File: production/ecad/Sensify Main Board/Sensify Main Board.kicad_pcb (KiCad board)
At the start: 4 copper layers, 142 parts, among them J1 1-2834011-3, J2 1-2834011-2, J3 1332645, J4 0532611271, J6 Conn_01x02_Socket, J7 Conn_01x02_Socket, J8 Conn_01x02_Socket, J9 Conn_01x02_Socket, Q1 2N700, Q2 PMPB13XNE,115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

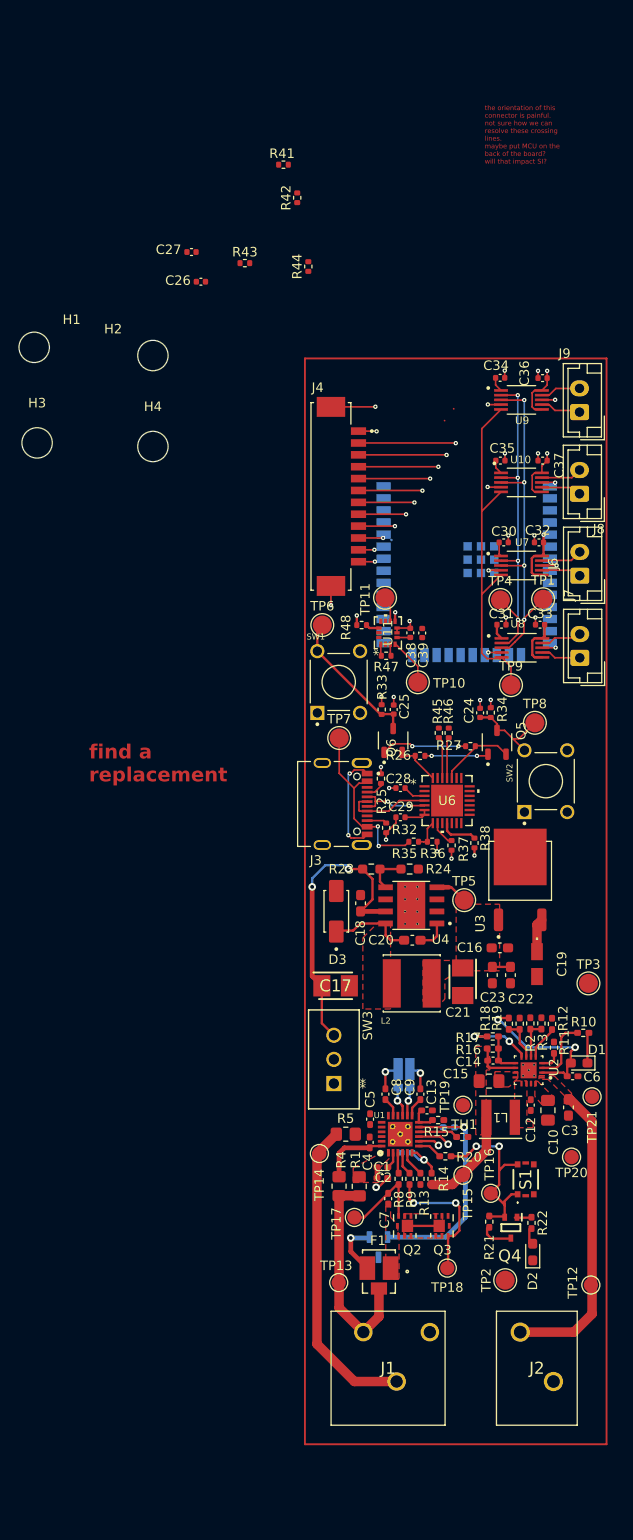
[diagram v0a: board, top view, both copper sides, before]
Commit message: main board layout
made some changes to routing, connected up parts of the MCU
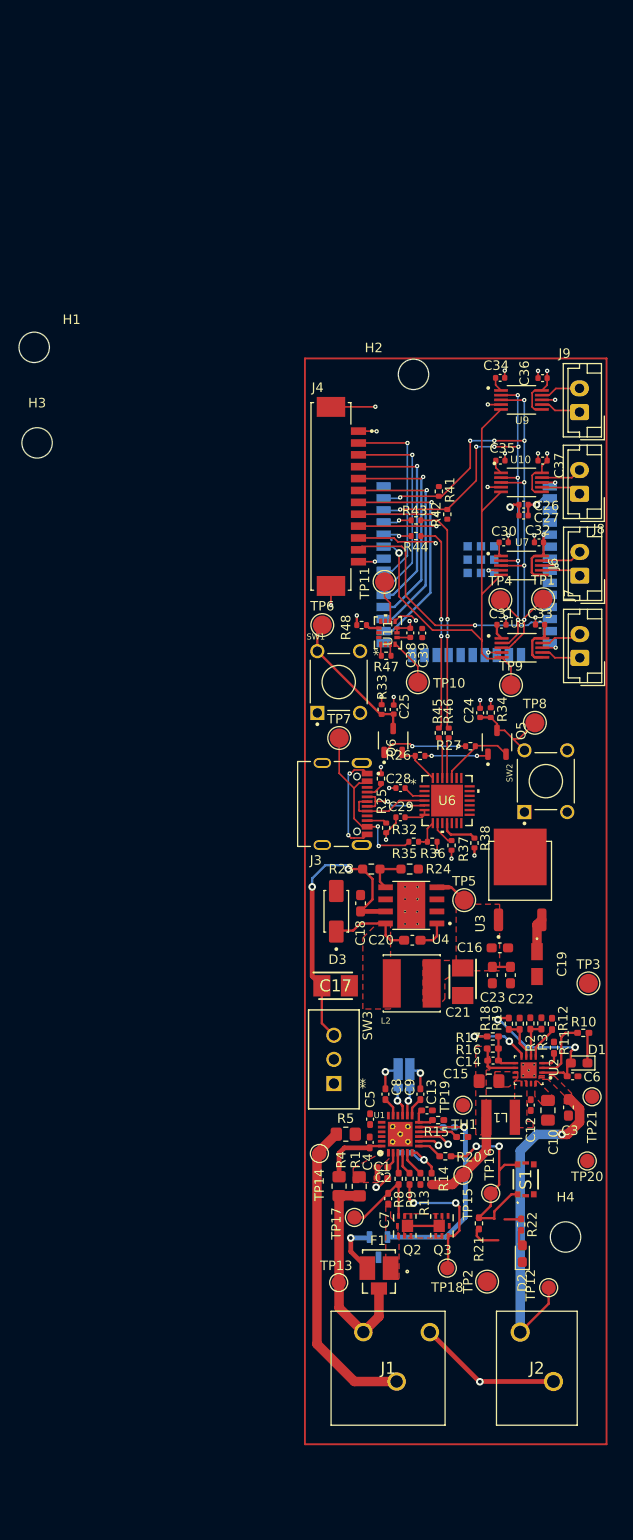
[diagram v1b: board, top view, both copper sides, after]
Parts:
- removed Q4: BSS223PWH6327XTSA1, Sensify Footprints:SOT65P210X100-3N
- moved H4 93.9 mm to (154.9, 162.1)
- moved C27 44.6 mm to (150.5, 86.1), turned to 180 degrees
- moved C26 41.3 mm to (150.5, 85.0), turned to 180 degrees
- moved R41 38.1 mm to (141.6, 83.6), turned to -90 degrees
- moved R42 36.9 mm to (142.5, 86.0)
- moved R43 32.5 mm to (139.2, 86.6), turned to 180 degrees
- moved R44 30.5 mm to (139.2, 88.3), turned to 180 degrees
- moved H2 27.5 mm to (138.9, 71.3)
- moved TP12 4.45 mm to (153.2, 167.4)
- moved TP2 1.91 mm to (146.7, 166.8)
- moved TP20 1.70 mm to (157.2, 154.1)
- moved TP11 1.68 mm to (135.9, 93.1)
- moved R22 1.10 mm to (150.3, 160.8)
- moved D2 1.10 mm to (150.4, 163.8)
- moved R21 1.10 mm to (145.8, 160.6)
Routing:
- net NovelDetect: track 1.68 -> 26.8 mm
- net UART_RXD: track 0.00 -> 24.1 mm, vias 0 -> 2
- net UART_TXD: track 0.00 -> 22.3 mm, vias 0 -> 2
- net SCL: track 37.7 -> 56.8 mm, vias 5 -> 9
- net SDA: track 41.9 -> 60.9 mm, vias 5 -> 9
- net NovelMechPin7: track 5.90 -> 23.9 mm
- net HAPTICS_EN: track 38.0 -> 55.6 mm, vias 0 -> 1
- net GND: track 54.5 -> 72.0 mm, vias 30 -> 32
- net NovelMechPin6: track 6.74 -> 23.2 mm
- net NovelMechPin5: track 7.54 -> 23.0 mm
- net NovelMechPin4: track 8.44 -> 21.8 mm
- net NovelMechPin3: track 9.28 -> 20.9 mm
- net NovelMechPin2: track 10.2 -> 20.2 mm
- net NovelMechPin10: track 2.59 -> 8.36 mm
- net +3V3: track 19.9 -> 25.2 mm, vias 7 -> 8
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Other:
- board text removed: "find a replacement"
- board text removed: "the orientation of this connector is painful. not sure how we can resolve these crossing lines. maybe put MCU on the back of the board? will that impact SI?"

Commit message: added last mounting hole and moved aronud R7 to make room for MH
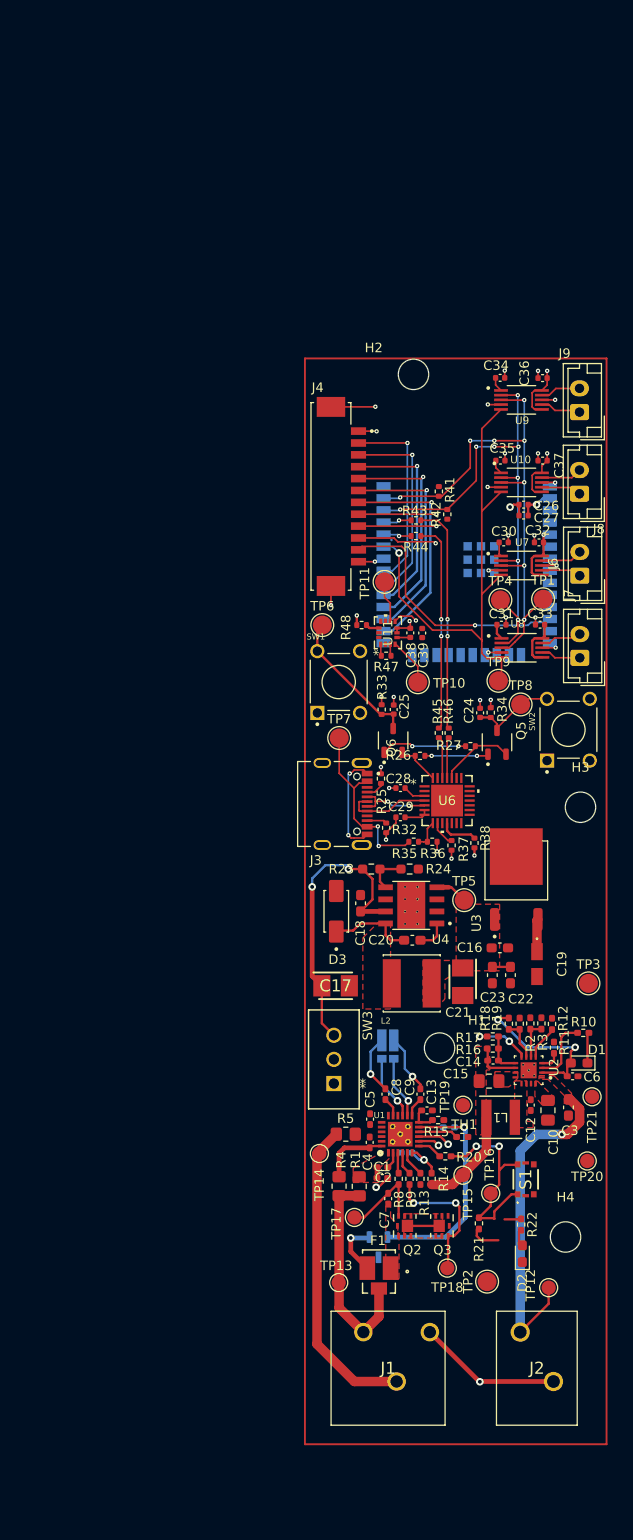
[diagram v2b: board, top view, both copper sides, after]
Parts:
- moved H1 85.2 mm to (141.7, 142.2)
- moved H3 68.9 mm to (156.5, 116.8)
- moved SW2 5.91 mm to (155.2, 108.7)
- moved R7 3.47 mm to (136.2, 142.0)
- moved TP8 2.44 mm to (150.2, 106.0)
- moved TP9 1.40 mm to (147.9, 103.5)
- moved U3 0.41 mm to (149.8, 124.5)
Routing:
- net GND: track 72.0 -> 78.4 mm
- net Net-(U1-CSP): track 3.03 -> 6.89 mm
- net Net-(U1-CSN): track 2.89 -> 6.66 mm
- net Net-(U2-FB_GND): track 7.42 -> 6.30 mm
- net HAPTICS_EN: track 55.6 -> 54.8 mm

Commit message: Main Board Layout
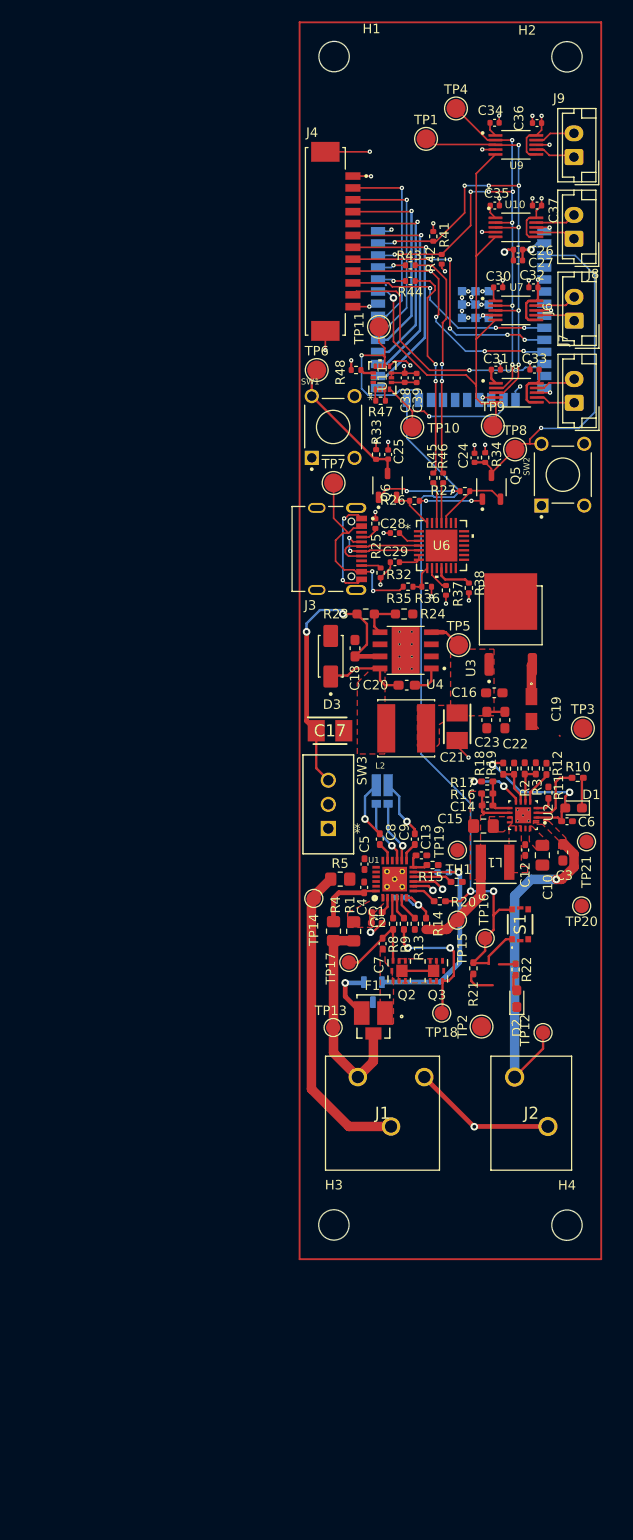
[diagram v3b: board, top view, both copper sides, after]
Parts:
- moved H1 105.0 mm to (130.6, 37.8)
- moved TP4 52.0 mm to (143.4, 43.3)
- moved H3 51.1 mm to (130.6, 160.8)
- moved TP1 50.0 mm to (140.3, 46.5)
- moved H2 37.1 mm to (155.1, 37.8)
- moved C16 26.9 mm to (147.4, 104.8)
- moved C15 26.9 mm to (146.3, 118.8)
- moved C18 26.9 mm to (132.8, 100.1)
- moved C19 26.9 mm to (151.4, 106.5)
- moved C20 26.9 mm to (138.2, 104.0)
- moved C21 26.9 mm to (143.5, 108.4)
- moved C22 26.9 mm to (148.6, 107.7)
- moved C23 26.9 mm to (146.7, 107.7)
- moved C25 26.9 mm to (136.3, 79.7)
- moved C28 26.9 mm to (137.0, 88.0)
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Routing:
- net BMS_ALERT: track 22.0 -> 81.7 mm
- net EN: track 9.53 -> 38.7 mm, vias 0 -> 1
- net GND: track 78.4 -> 100.2 mm, vias 32 -> 43
- net NovelMechPin8: track 8.20 -> 27.9 mm, vias 1 -> 5
- net NovelMechPin9: track 8.21 -> 26.7 mm, vias 1 -> 4
- net NovelMechPin10: track 8.36 -> 22.8 mm, vias 1 -> 3
- net INTERRUPT2_IMU: track 4.40 -> 17.9 mm, vias 0 -> 1
- net INTERRUPT1_IMU: track 5.21 -> 16.3 mm, vias 0 -> 1
- net SDA: track 60.9 -> 65.6 mm
- net SCL: track 56.8 -> 59.9 mm
- net +3V3: track 25.1 -> 28.1 mm, vias 8 -> 10
- net USB_D-: track 8.05 -> 10.2 mm
- net FLASHING_VBUS_5V: track 19.3 -> 21.4 mm
- net USB_D+: track 9.22 -> 10.3 mm
- net UART_TXD: track 22.3 -> 22.9 mm

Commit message: routing generally done
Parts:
- removed C13: 0.47u, Capacitor_SMD:C_0402_1005Metric_Pad0.74x0.62mm_HandSolder
- removed R12, R3: 0, Resistor_SMD:R_0402_1005Metric_Pad0.72x0.64mm_HandSolder
- added Q4: BSS223PWH6327XTSA1, Sensify Footprints:SOT65P210X100-3N, F.Cu at (148.0, 161.2)
- R7: moved to F.Cu
- moved H3 88.1 mm to (99.3, 78.5)
- moved TP4 52.0 mm to (148.1, 95.0)
- moved TP1 49.9 mm to (152.7, 94.8)
- moved H1 44.0 mm to (99.0, 68.4)
- moved H2 37.1 mm to (138.9, 71.3)
- moved SW2 32.3 mm to (152.9, 114.1)
- moved R7 30.9 mm to (137.5, 146.0), turned to 180 degrees
- moved TP8 28.9 mm to (151.7, 108.0)
- moved C29 27.5 mm to (138.9, 118.4), turned to -90 degrees
- moved C9 27.4 mm to (139.6, 147.6)
- moved TP9 27.4 mm to (149.2, 104.0)
- moved C8 27.3 mm to (135.4, 147.5)
- moved C28 27.3 mm to (138.8, 115.2), turned to -90 degrees
- moved R38 27.0 mm to (145.8, 120.7)
- moved R24 27.0 mm to (139.0, 123.5)
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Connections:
- R15 pad 1: AOLDO_OUT -> Net-(U1-AOLDO)
- R2 pad 1: AOLDO_OUT -> Net-(U2-~{EN})
- R2 pad 2: /BMS/CHARGER_EN -> GND
- R7 pad 2: Net-(U1-CSP) -> Net-(U1-CSN)
- R7 pad 3: Net-(U1-CSN) -> Net-(U1-CSP)
- U1 pad 12: AOLDO_OUT -> Net-(U1-AOLDO)
- U2 pad 5: Net-(U2-POL) -> unconnected-(U2-POL-Pad5)
- U2 pad 6: /BMS/CHARGER_EN -> Net-(U2-~{EN})
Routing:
- net GND: track 100.2 -> 180.9 mm, vias 43 -> 67
- net SDA: track 65.6 -> 141.5 mm, vias 9 -> 11
- net SCL: track 59.9 -> 134.6 mm, vias 9 -> 11
- net PACK+: track 16.3 -> 44.4 mm
- net INTERRUPT2_IMU: track 17.9 -> 4.40 mm, vias 1 -> 0
- net +3V3: track 28.1 -> 38.6 mm, vias 10 -> 14
- net Net-(U2-PMID): track 0.00 -> 9.96 mm
- net IO0: track 15.3 -> 23.6 mm
- net Net-(U1-TH1): track 4.20 -> 11.9 mm
- net USB_9V+: track 35.6 -> 41.9 mm
- net Net-(U1-CELL1): track 0.00 -> 6.14 mm
- net Net-(U1-CSN): track 6.66 -> 2.03 mm, vias 1 -> 0
- net Net-(U1-CSP): track 6.89 -> 2.34 mm, vias 1 -> 0
- net /BMS/CHARGER_EN: track 4.15 -> 0.00 mm
- net +5V: track 30.8 -> 34.8 mm, vias 4 -> 6
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- added copper zone on In1.Cu, net +3V3
- added copper zone on In1.Cu, net +5V
- added copper zone on B.Cu, net GND
- added copper zone on In2.Cu, net GND
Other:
- board outline added: 31.8 x 114.3 mm

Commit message: mounting holes...
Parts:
- moved H1 124.2 mm to (131.0, 188.4)
- moved H3 34.3 mm to (130.9, 91.9)
- moved H2 26.7 mm to (155.9, 91.9)
- moved H4 26.4 mm to (155.8, 188.4)
- moved U5 12.6 mm to (143.3, 75.8)
- moved C26 7.62 mm to (150.5, 77.4)
- moved C27 7.62 mm to (150.5, 78.5)
- moved C30 7.62 mm to (148.4, 81.3)
- moved C32 7.62 mm to (152.1, 81.3)
- moved C34 7.62 mm to (148.1, 64.0)
- moved C35 7.62 mm to (148.1, 72.7)
- moved C37 7.62 mm to (152.5, 72.7)
- moved J6 7.62 mm to (156.4, 84.8)
- moved J8 7.62 mm to (156.4, 76.2)
- moved R41 7.62 mm to (141.6, 76.0)
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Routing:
- net SDA: track 141.5 -> 55.0 mm, vias 11 -> 1
- net SCL: track 134.6 -> 53.7 mm, vias 11 -> 1
- net HAPTICS_EN: track 56.1 -> 0.00 mm, vias 1 -> 0
- net GND: track 180.9 -> 130.8 mm, vias 67 -> 36
- net NovelDetect: track 27.2 -> 0.00 mm, vias 1 -> 0
- net NovelMechPin8: track 26.6 -> 0.00 mm, vias 1 -> 0
- net NovelMechPin9: track 25.8 -> 0.00 mm, vias 1 -> 0
- net NovelMechPin10: track 25.3 -> 0.00 mm, vias 3 -> 0
- net +5V: track 34.8 -> 10.5 mm, vias 6 -> 3
- net IO0: track 23.6 -> 2.20 mm
- net +3V3: track 38.6 -> 20.5 mm, vias 14 -> 5
- net INTERRUPT1_IMU: track 16.3 -> 0.00 mm, vias 1 -> 0
- net NovelMechPin7: track 23.9 -> 8.99 mm
- net NovelMechPin6: track 23.2 -> 9.37 mm
- net NovelMechPin5: track 23.0 -> 9.36 mm
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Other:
- board size 31.8 x 114.3 mm -> 31.8 x 130 mm

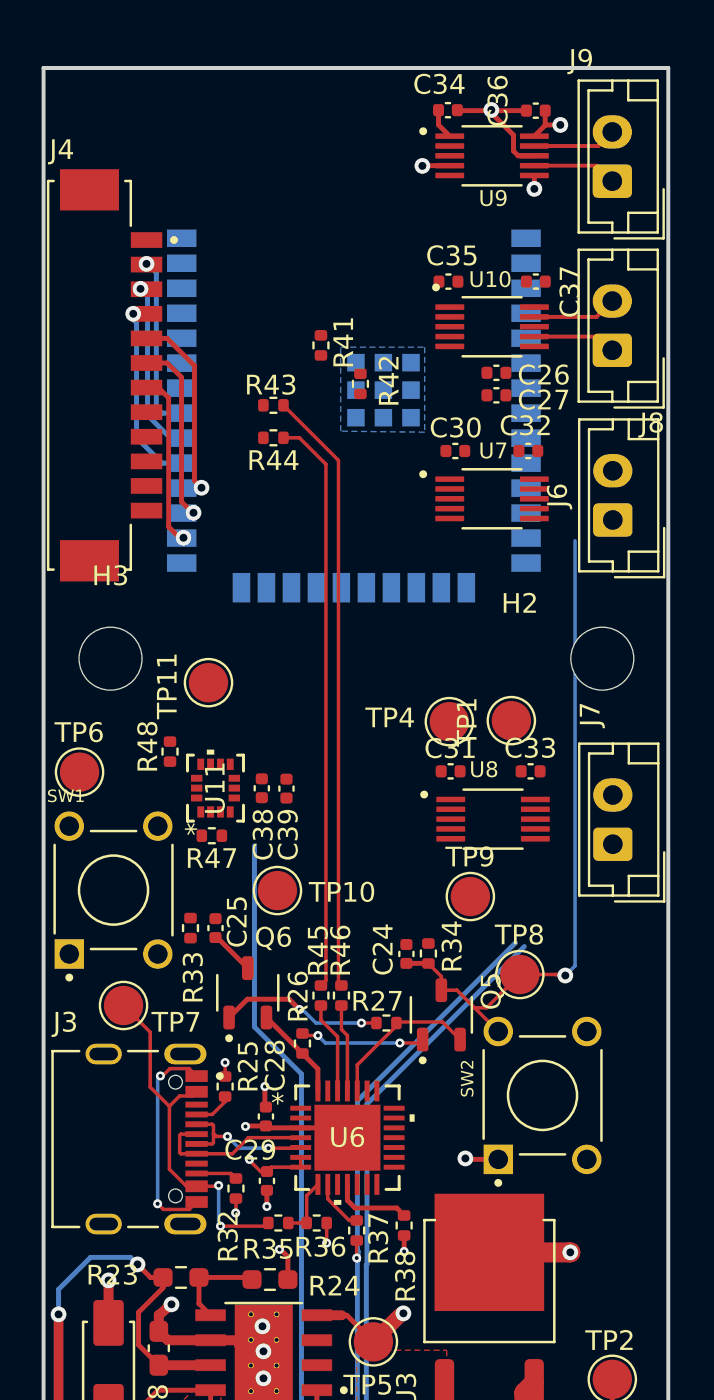
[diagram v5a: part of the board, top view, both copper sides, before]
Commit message: Everything UART and above is error free
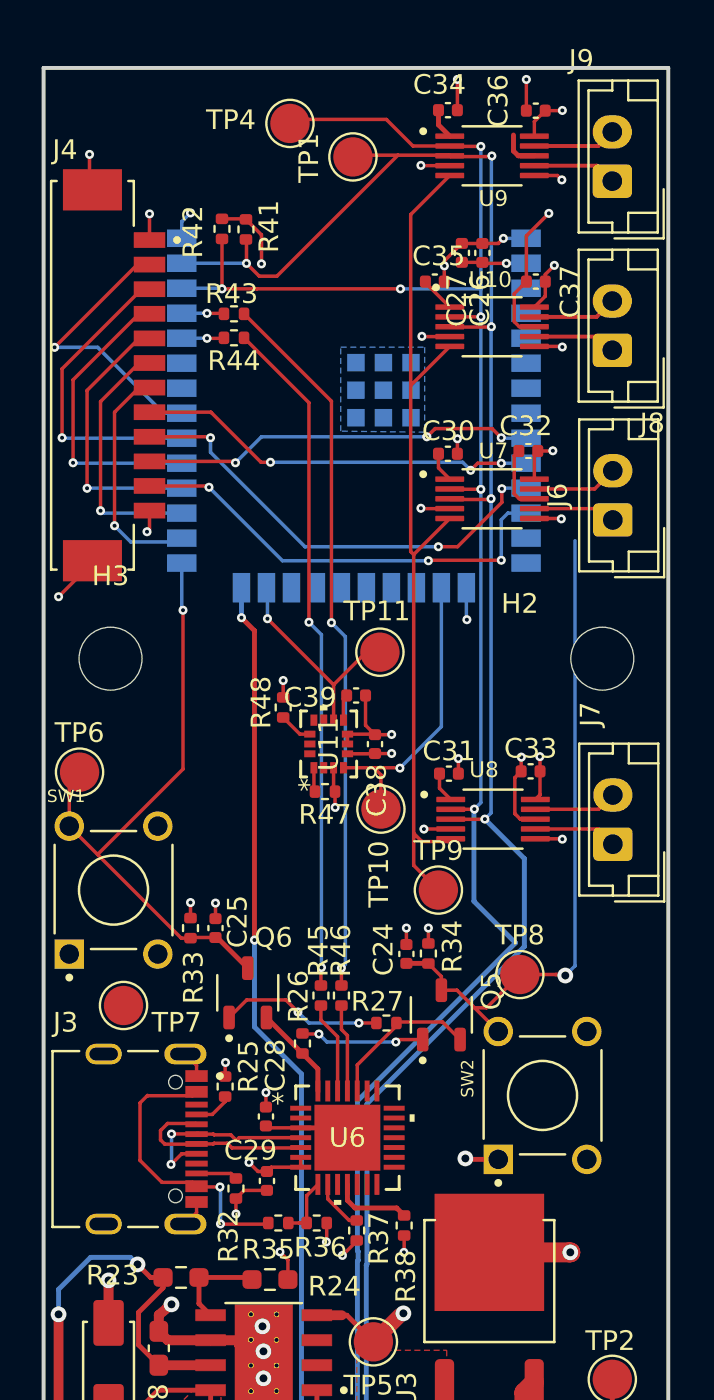
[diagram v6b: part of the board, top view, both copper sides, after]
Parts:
- moved TP4 31.5 mm to (140.0, 64.7)
- moved TP1 29.8 mm to (143.2, 66.4)
- moved R42 10.6 mm to (136.6, 70.1), turned to -90 degrees
- moved TP11 8.85 mm to (144.6, 91.6), turned to 0 degrees
- moved C27 7.45 mm to (148.8, 71.3), turned to 90 degrees
- moved R41 7.02 mm to (137.8, 70.1)
- moved TP10 6.69 mm to (144.7, 99.5), turned to 0 degrees
- moved C38 6.17 mm to (144.4, 96.2)
- moved R47 6.17 mm to (141.8, 98.7)
- moved R48 6.17 mm to (139.7, 94.4)
- moved U11 6.17 mm to (142.0, 96.2)
- moved C26 6.14 mm to (149.8, 71.3), turned to 90 degrees
- moved C39 5.91 mm to (143.4, 93.8), turned to 0 degrees
- moved R44 5.46 mm to (137.2, 75.6)
- moved R43 5.06 mm to (137.2, 74.4)
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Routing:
- net SCL: track 53.7 -> 127.7 mm, vias 1 -> 7
- net SDA: track 55.0 -> 124.3 mm, vias 1 -> 6
- net HAPTICS_EN: track 0.00 -> 45.2 mm
- net GND: track 130.8 -> 160.9 mm, vias 36 -> 49
- net IO0: track 2.20 -> 31.6 mm, vias 0 -> 1
- net NovelMechPin9: track 0.00 -> 23.5 mm, vias 0 -> 3
- net NovelDetect: track 0.00 -> 22.9 mm, vias 0 -> 3
- net NovelMechPin8: track 0.00 -> 20.5 mm, vias 0 -> 3
- net NovelMechPin10: track 0.00 -> 20.1 mm, vias 0 -> 3
- net +3V3: track 20.5 -> 37.3 mm, vias 5 -> 13
- net INTERRUPT1_IMU: track 0.00 -> 15.2 mm, vias 0 -> 1
- net +5V: track 10.5 -> 24.0 mm, vias 3 -> 10
- net BMS_ALERT: track 78.8 -> 92.2 mm, vias 2 -> 4
- net INTERRUPT2_IMU: track 0.00 -> 11.2 mm, vias 0 -> 1
- net NovelMechPin3: track 8.79 -> 16.3 mm
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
